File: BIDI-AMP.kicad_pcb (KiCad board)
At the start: 2 copper layers, 48.3 x 33 mm, 31 parts, among them J1 Conn_01x03, J2 Conn_01x01, J3 Conn_01x01, Q1 Q_NPN_EBC, Q2 Q_NPN_EBC

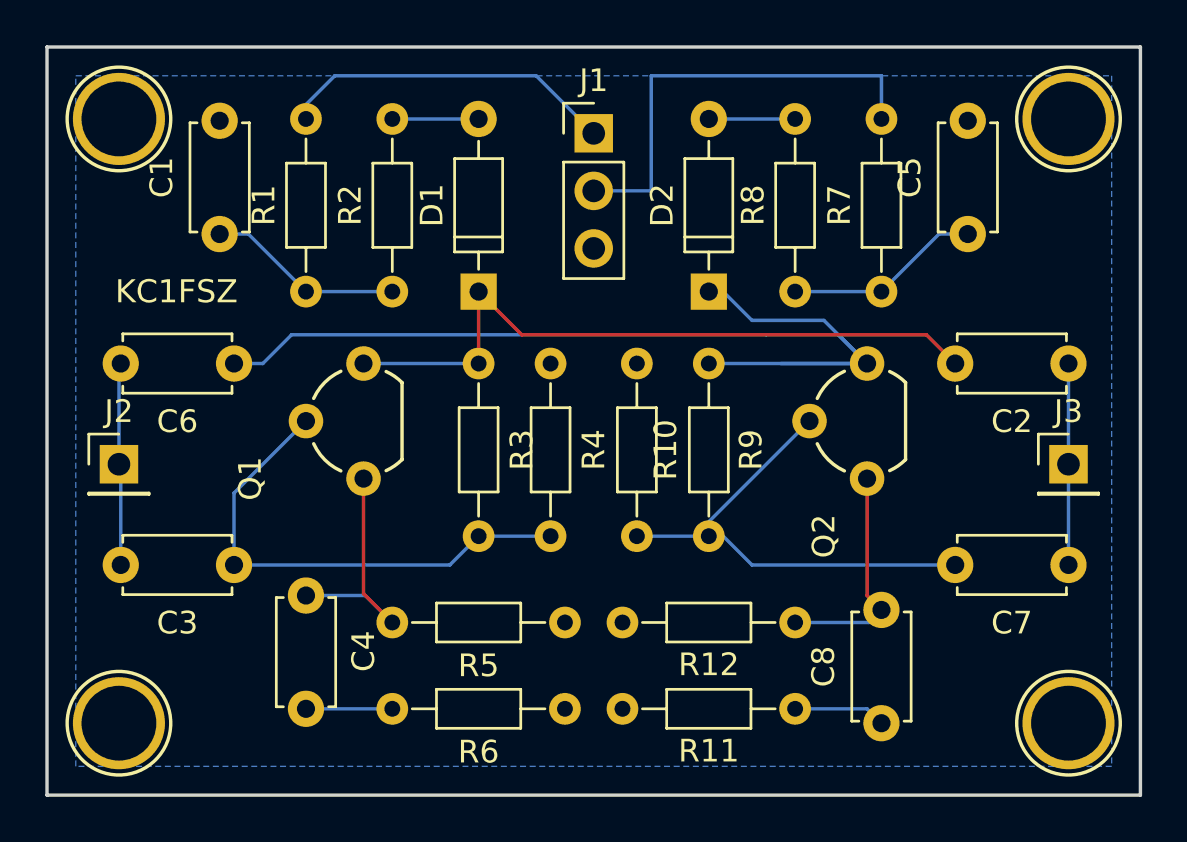
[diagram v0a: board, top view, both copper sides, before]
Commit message: New layout (ground)
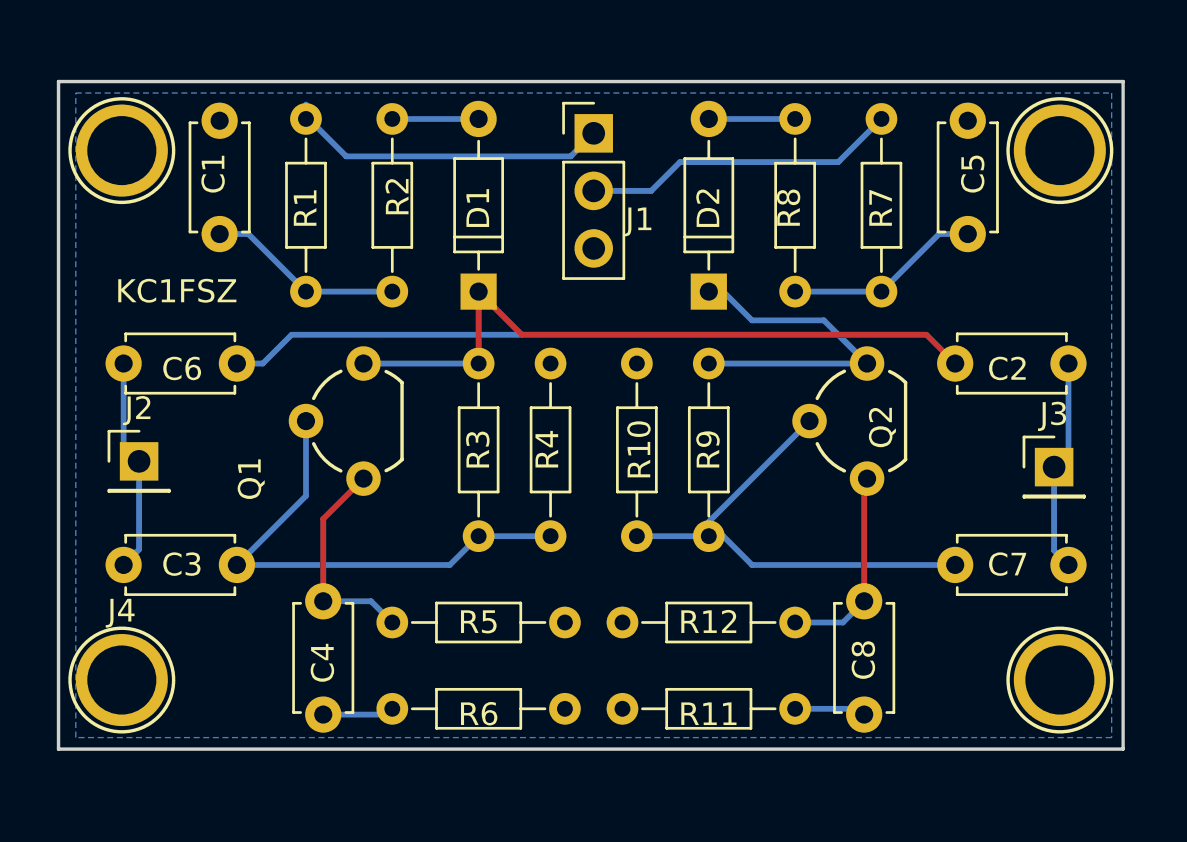
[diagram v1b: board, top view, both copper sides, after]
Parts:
- removed the REF** at (151.8, 113.7)
- added J4: Conn_01x01, Connectors:1pin, F.Cu at (151.9, 111.8)
- moved REF** 1.94 mm to (193.3, 111.8)
- moved REF** 1.45 mm to (193.3, 88.4)
- moved REF** 1.40 mm to (151.9, 88.4)
- moved J2 0.90 mm to (152.7, 102.1)
- moved C8 0.85 mm to (184.7, 113.3)
- moved C4 0.80 mm to (160.8, 113.3)
- moved J3 0.65 mm to (193.0, 102.4)
- moved C3 0.13 mm to (157.0, 106.7)
- moved C6 0.13 mm to (157.0, 97.8)
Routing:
- net TX_PWR: track 19.7 -> 14.0 mm
- net Net-(C6-Pad1): track 48.1 -> 44.3 mm
- net Net-(C4-Pad2): track 11.2 -> 9.59 mm
- net RF_LEFT: track 8.96 -> 10.2 mm
- net Net-(C8-Pad2): track 10.1 -> 8.90 mm
- net Net-(C8-Pad1): track 4.07 -> 3.15 mm
- net Net-(C4-Pad1): track 3.81 -> 3.15 mm
- net RF_RIGHT: track 8.89 -> 9.42 mm
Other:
- board size 48.3 x 33 mm -> 47 x 29.5 mm
- net class Default: clearance 0.01 -> 0.254; trace_width 0.01 -> 0.254; via_dia 0.027 -> 0.6858; via_drill 0.013 -> 0.3302
- rule trace_clearance: 0.01 -> 0.254
- rule trace_min: 0.01 -> 0.254
- rule via_min_drill: 0.013 -> 0.3302
- rule via_min_size: 0.027 -> 0.6858
- board text added: "2018-07 v2"
